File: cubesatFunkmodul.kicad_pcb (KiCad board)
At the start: 4 copper layers, 85 x 85 mm, 207 parts, among them CON11 DISCO-CON1, CON21 DISCO-CON2, Q1 SSM3J334RLFTR-ND, Q10 AO3414, Q11 MMBT5551-TP, Q12 MMBT5551-TP, Q13 MMBT5551-TP, Q14 MMBT5551-TP, Q15 MMBT5551-TP, Q16 MMBT5551-TP, Q17 AO3414, Q18 AO3414, Q2 AO3414, Q3 MMBT5551-TP, Q4 MMBT5551-TP, Q5 MMBT5551-TP, Q6 MMBT5551-TP, Q7 MMBT5551-TP, Q8 MMBT5551-TP, Q9 SSM3J334RLFTR-ND, U1 MC74HC4538A, U10 RFM23BP, U2 MAX892, U3 ATMEGA128-16AU, U4 LTC3113, U5 RFM23BP, U6 MC74HC4538A, U7 MAX892, U8 ATMEGA128-16AU, U9 LTC3113, Y1 Crystal_GND24, Y2 Crystal_GND24

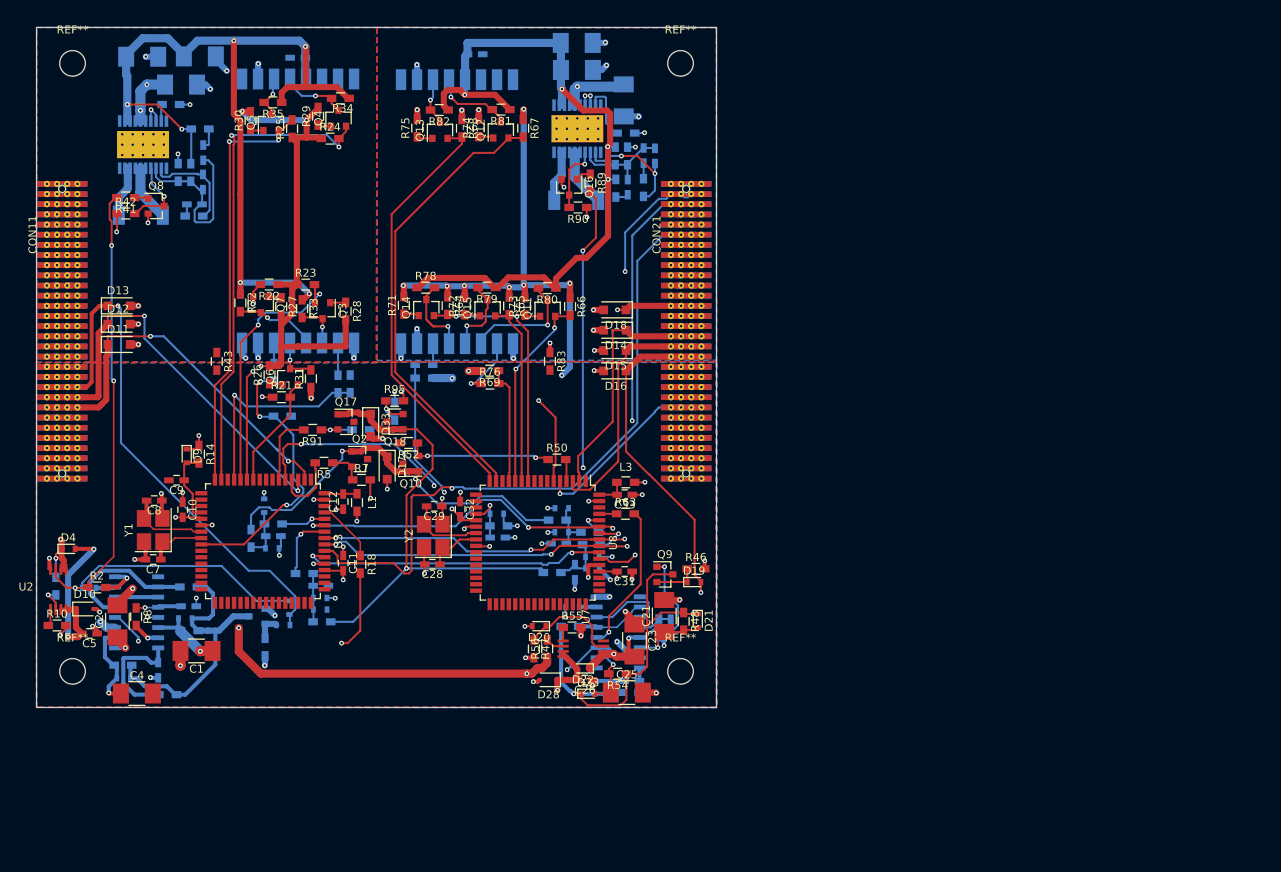
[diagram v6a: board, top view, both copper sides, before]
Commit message: Adds SMA and Burnwire connectors
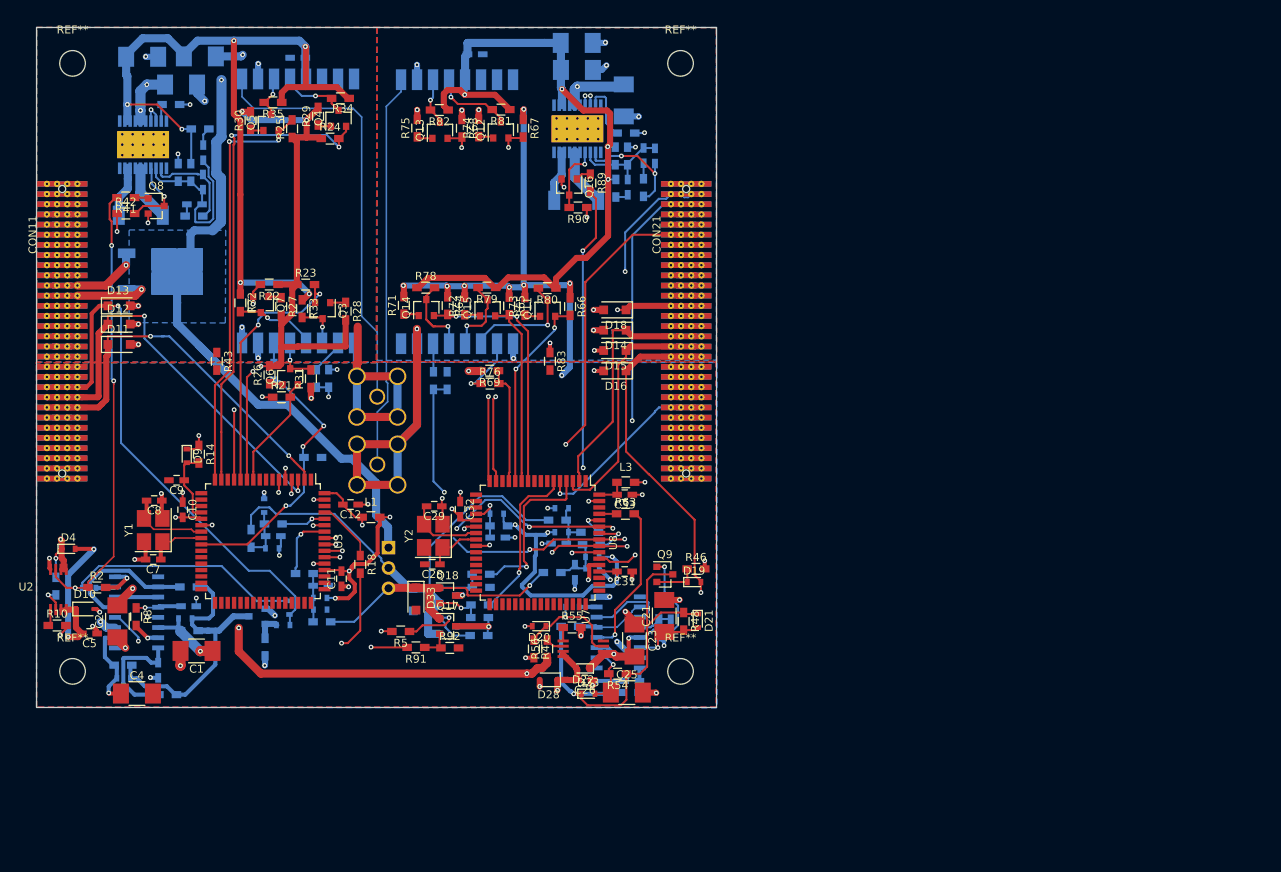
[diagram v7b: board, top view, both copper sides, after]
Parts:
- added AE1: Antenna, Connectors:SMA_THT_Jack_Straight, B.Cu at (93.6, 80.1)
- added AE2: Antenna, Connectors:SMA_THT_Jack_Straight, B.Cu at (93.6, 88.6)
- added D34: STPS640CBY-TR, TO_SOT_Packages_SMD:TO-252-2, B.Cu at (66.5, 64.5)
- added J1: Conn_01x03, Pin_Headers:Pin_Header_Straight_1x03_Pitch2.54mm, B.Cu at (95.0, 99.0)
- D17, Q10, Q2, R50, R52, R7, R95: moved to B.Cu
- R92: moved to F.Cu
- moved R91 30.1 mm to (98.4, 111.5)
- moved R92 29.4 mm to (102.7, 111.6)
- moved Q17 28.5 mm to (102.4, 108.8)
- moved R96 27.9 mm to (106.4, 107.8), turned to 0 degrees
- moved R95 27.6 mm to (106.4, 106.2)
- moved R7 24.4 mm to (106.3, 110.0)
- moved Q2 23.6 mm to (102.4, 108.9)
- moved R5 23.2 mm to (96.5, 109.5)
- moved Q18 22.7 mm to (102.4, 105.0), turned to 0 degrees
- moved D33 22.4 mm to (98.4, 105.4)
- moved R52 20.2 mm to (106.6, 104.0), turned to 0 degrees
- moved R50 17.2 mm to (106.5, 102.3)
- moved Q10 17.1 mm to (102.4, 105.0), turned to 0 degrees
- moved D17 16.8 mm to (98.1, 105.5)
- moved R44 6.41 mm to (85.5, 87.7)
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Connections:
- net Net-(CON21-Pad12) renamed /Connector/3V3_Reset
- CON11 pad 11: Net-(CON11-Pad11) -> /Connector/BAT1
- CON11 pad 12: Net-(CON11-Pad12) -> /Connector/BAT2
- U1 pad 9: (no net) -> Net-(U1-Pad9)
- U10 pad 14: (no net) -> Net-(U10-Pad14)
- U10 pad 15: (no net) -> Net-(U10-Pad15)
- U10 pad 16: (no net) -> Net-(U10-Pad16)
- U10 pad 9: (no net) -> Net-(AE2-Pad1)
- U3 pad 1: (no net) -> Net-(U3-Pad1)
- U3 pad 14: (no net) -> Net-(U3-Pad14)
- U3 pad 17: (no net) -> Net-(U3-Pad17)
- U3 pad 18: (no net) -> Net-(U3-Pad18)
- U3 pad 19: (no net) -> Net-(U3-Pad19)
- U3 pad 26: (no net) -> Net-(U3-Pad26)
- U3 pad 27: (no net) -> Net-(U3-Pad27)
- U3 pad 28: (no net) -> Net-(U3-Pad28)
- U3 pad 29: (no net) -> Net-(U3-Pad29)
- U3 pad 30: (no net) -> Net-(U3-Pad30)
- U3 pad 31: (no net) -> Net-(U3-Pad31)
- U3 pad 32: (no net) -> Net-(U3-Pad32)
- U3 pad 33: (no net) -> Net-(U3-Pad33)
- U3 pad 34: (no net) -> Net-(U3-Pad34)
- U3 pad 35: (no net) -> Net-(U3-Pad35)
- U3 pad 36: (no net) -> Net-(U3-Pad36)
- U3 pad 37: (no net) -> Net-(U3-Pad37)
- U3 pad 38: (no net) -> Net-(U3-Pad38)
- U3 pad 39: (no net) -> Net-(U3-Pad39)
- U3 pad 40: (no net) -> Net-(U3-Pad40)
- U3 pad 41: (no net) -> Net-(U3-Pad41)
- U3 pad 42: (no net) -> Net-(U3-Pad42)
- U3 pad 43: (no net) -> Net-(U3-Pad43)
- U3 pad 44: (no net) -> Net-(U3-Pad44)
- U3 pad 45: (no net) -> Net-(U3-Pad45)
- U3 pad 46: (no net) -> Net-(U3-Pad46)
- U3 pad 47: (no net) -> Net-(U3-Pad47)
- U3 pad 48: (no net) -> Net-(U3-Pad48)
- U3 pad 49: (no net) -> Net-(U3-Pad49)
- U3 pad 50: (no net) -> Net-(U3-Pad50)
- U3 pad 51: (no net) -> Net-(U3-Pad51)
- U3 pad 62: (no net) -> Net-(U3-Pad62)
- U3 pad 7: (no net) -> Net-(U3-Pad7)
- U3 pad 8: (no net) -> Net-(U3-Pad8)
- U3 pad 9: (no net) -> Net-(U3-Pad9)
- U5 pad 14: (no net) -> Net-(U5-Pad14)
- U5 pad 15: (no net) -> Net-(U5-Pad15)
- U5 pad 16: (no net) -> Net-(U5-Pad16)
- U5 pad 9: (no net) -> Net-(AE1-Pad1)
- U6 pad 9: (no net) -> Net-(U6-Pad9)
- U8 pad 1: (no net) -> Net-(U8-Pad1)
- U8 pad 14: (no net) -> Net-(U8-Pad14)
- U8 pad 17: (no net) -> Net-(U8-Pad17)
- U8 pad 18: (no net) -> Net-(U8-Pad18)
- U8 pad 19: (no net) -> Net-(U8-Pad19)
- U8 pad 26: (no net) -> Net-(U8-Pad26)
- U8 pad 27: (no net) -> Net-(U8-Pad27)
- U8 pad 28: (no net) -> Net-(U8-Pad28)
- U8 pad 29: (no net) -> Net-(U8-Pad29)
- U8 pad 30: (no net) -> Net-(U8-Pad30)
- U8 pad 31: (no net) -> Net-(U8-Pad31)
- U8 pad 32: (no net) -> Net-(U8-Pad32)
- U8 pad 33: (no net) -> Net-(U8-Pad33)
- U8 pad 34: (no net) -> Net-(U8-Pad34)
- U8 pad 35: (no net) -> Net-(U8-Pad35)
- U8 pad 36: (no net) -> Net-(U8-Pad36)
- U8 pad 37: (no net) -> Net-(U8-Pad37)
- U8 pad 38: (no net) -> Net-(U8-Pad38)
- U8 pad 39: (no net) -> Net-(U8-Pad39)
- U8 pad 40: (no net) -> Net-(U8-Pad40)
- U8 pad 41: (no net) -> Net-(U8-Pad41)
- U8 pad 42: (no net) -> Net-(U8-Pad42)
- U8 pad 43: (no net) -> Net-(U8-Pad43)
- U8 pad 44: (no net) -> Net-(U8-Pad44)
- U8 pad 45: (no net) -> Net-(U8-Pad45)
- U8 pad 46: (no net) -> Net-(U8-Pad46)
- U8 pad 47: (no net) -> Net-(U8-Pad47)
- U8 pad 48: (no net) -> Net-(U8-Pad48)
- U8 pad 49: (no net) -> Net-(U8-Pad49)
- U8 pad 50: (no net) -> Net-(U8-Pad50)
- U8 pad 51: (no net) -> Net-(U8-Pad51)
- U8 pad 62: (no net) -> Net-(U8-Pad62)
- U8 pad 7: (no net) -> Net-(U8-Pad7)
- U8 pad 8: (no net) -> Net-(U8-Pad8)
- U8 pad 9: (no net) -> Net-(U8-Pad9)
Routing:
- net VBAT: track 114.1 -> 194.4 mm, vias 5 -> 6
- net Net-(AE1-Pad1): track 0.00 -> 54.0 mm
- net Net-(AE2-Pad1): track 0.00 -> 49.5 mm
- net /Funkmodul2/Funkeinheit2/PGND: track 14.0 -> 61.5 mm, vias 8 -> 7
- net /Funkmodul1/Funkeinheit/PGND: track 13.6 -> 44.5 mm, vias 7 -> 6
- net /Funkmodul2/VCC: track 104.1 -> 132.3 mm
- net WIRE_CONN2: track 60.3 -> 34.7 mm
- net /Funkmodul1/BURNWIRE2: track 8.79 -> 30.5 mm, vias 0 -> 2
- net /Funkmodul2/BURNWIRE: track 2.73 -> 20.7 mm, vias 0 -> 1
- net /Funkmodul1/BURNWIRE: track 8.31 -> 25.0 mm, vias 0 -> 2
- net /Funkmodul1/VCC: track 100.6 -> 115.3 mm
- net /Connector/BAT2: track 0.00 -> 12.7 mm, vias 0 -> 1
- net Net-(Q10-Pad2): track 18.1 -> 5.74 mm, vias 2 -> 0
- net WIRE_CONN: track 49.7 -> 61.6 mm, vias 2 -> 0
- net /Funkmodul2/Funkeinheit2/RXON: track 57.4 -> 45.8 mm, vias 0 -> 2
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- added copper zone on In2.Cu, net /Funkmodul1/Funkeinheit/PGND
- added copper zone on In2.Cu, net /Funkmodul2/Funkeinheit2/PGND
- added copper zone on B.Cu, net VBAT

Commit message: Adds stiching vias
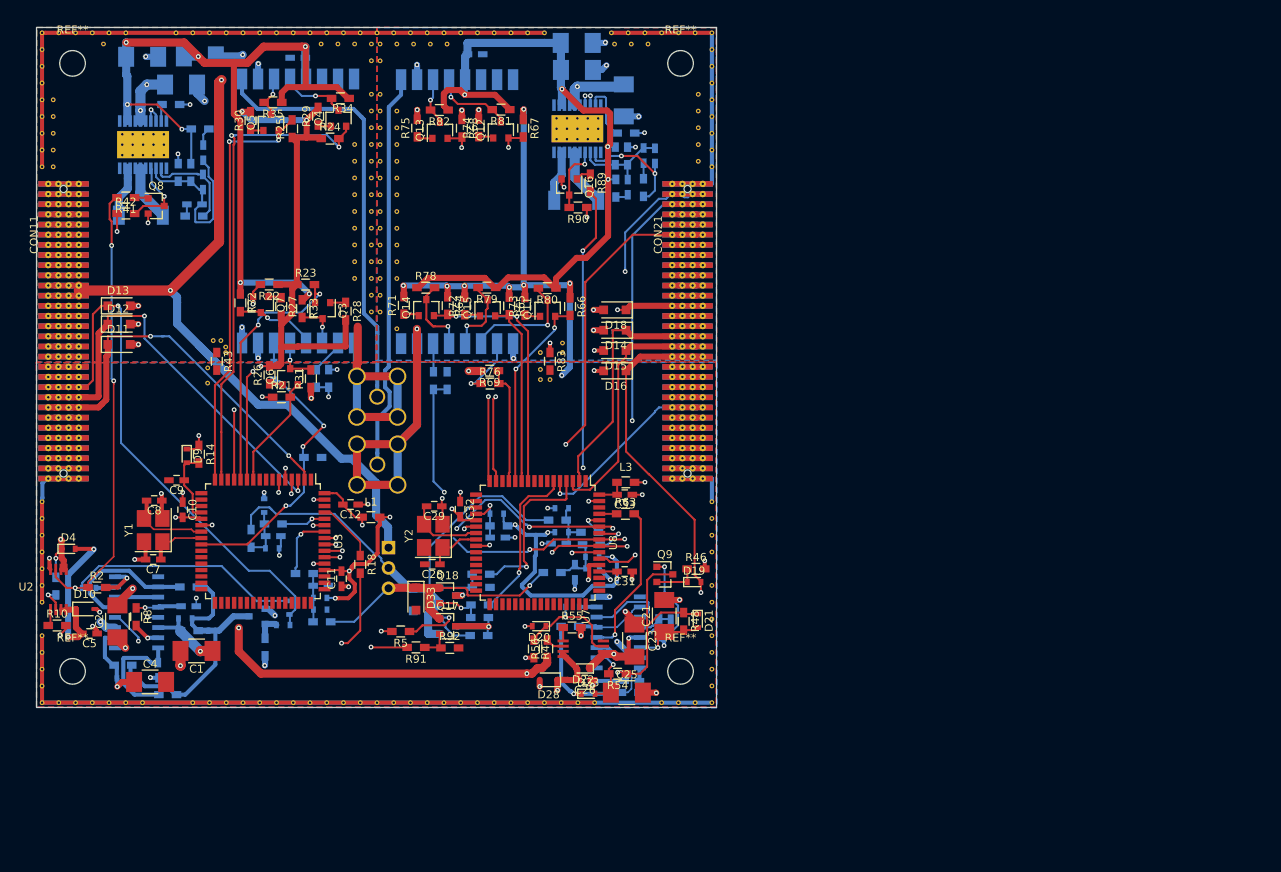
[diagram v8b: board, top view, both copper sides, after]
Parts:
- removed D34: STPS640CBY-TR, TO_SOT_Packages_SMD:TO-252-2
- added REF**: VIA-0.6, connect-sm:VIA-0.6, F.Cu at (115.2, 78.0)
- added REF**: VIA-0.6, connect-sm:VIA-0.6, F.Cu at (74.6, 74.6)
- added REF**: VIA-0.6, connect-sm:VIA-0.6, F.Cu at (51.7, 110.0)
- added REF**: VIA-0.6, connect-sm:VIA-0.6, F.Cu at (51.7, 112.1)
- added REF**: VIA-0.6, connect-sm:VIA-0.6, F.Cu at (51.7, 114.2)
- added REF**: VIA-0.6, connect-sm:VIA-0.6, F.Cu at (51.7, 116.3)
- added REF**: VIA-0.6, connect-sm:VIA-0.6, F.Cu at (51.7, 118.4)
- added REF**: VIA-0.6, connect-sm:VIA-0.6, F.Cu at (53.8, 118.4)
- added REF**: VIA-0.6, connect-sm:VIA-0.6, F.Cu at (55.9, 118.4)
- added REF**: VIA-0.6, connect-sm:VIA-0.6, F.Cu at (58.0, 118.4)
- added REF**: VIA-0.6, connect-sm:VIA-0.6, F.Cu at (60.1, 118.4)
- added REF**: VIA-0.6, connect-sm:VIA-0.6, F.Cu at (62.2, 118.4)
- added REF**: VIA-0.6, connect-sm:VIA-0.6, F.Cu at (74.0, 73.1)
- added REF**: VIA-0.6, connect-sm:VIA-0.6, F.Cu at (64.2, 118.4)
- added REF**: VIA-0.6, connect-sm:VIA-0.6, F.Cu at (70.5, 118.4)
- added REF**: VIA-0.6, connect-sm:VIA-0.6, F.Cu at (72.6, 118.4)
- added REF**: VIA-0.6, connect-sm:VIA-0.6, F.Cu at (74.7, 118.4)
- added REF**: VIA-0.6, connect-sm:VIA-0.6, F.Cu at (76.8, 118.4)
- added REF**: VIA-0.6, connect-sm:VIA-0.6, F.Cu at (78.9, 118.4)
- added REF**: VIA-0.6, connect-sm:VIA-0.6, F.Cu at (81.0, 118.4)
- added REF**: VIA-0.6, connect-sm:VIA-0.6, F.Cu at (83.1, 118.4)
- added REF**: VIA-0.6, connect-sm:VIA-0.6, F.Cu at (85.2, 118.4)
- added REF**: VIA-0.6, connect-sm:VIA-0.6, F.Cu at (87.3, 118.4)
- added REF**: VIA-0.6, connect-sm:VIA-0.6, F.Cu at (133.7, 50.7)
- added REF**: VIA-0.6, connect-sm:VIA-0.6, F.Cu at (89.4, 118.4)
- added REF**: VIA-0.6, connect-sm:VIA-0.6, F.Cu at (91.5, 118.4)
- added REF**: VIA-0.6, connect-sm:VIA-0.6, F.Cu at (93.6, 118.4)
- added REF**: VIA-0.6, connect-sm:VIA-0.6, F.Cu at (95.6, 118.4)
- added REF**: VIA-0.6, connect-sm:VIA-0.6, F.Cu at (97.7, 118.4)
- added REF**: VIA-0.6, connect-sm:VIA-0.6, F.Cu at (99.8, 118.4)
- added REF**: VIA-0.6, connect-sm:VIA-0.6, F.Cu at (101.9, 118.4)
- added REF**: VIA-0.6, connect-sm:VIA-0.6, F.Cu at (104.0, 118.4)
- added REF**: VIA-0.6, connect-sm:VIA-0.6, F.Cu at (106.1, 118.4)
- added REF**: VIA-0.6, connect-sm:VIA-0.6, F.Cu at (108.2, 118.4)
- added REF**: VIA-0.6, connect-sm:VIA-0.6, F.Cu at (133.7, 48.6)
- added REF**: VIA-0.6, connect-sm:VIA-0.6, F.Cu at (110.3, 118.4)
- added REF**: VIA-0.6, connect-sm:VIA-0.6, F.Cu at (112.4, 118.4)
- added REF**: VIA-0.6, connect-sm:VIA-0.6, F.Cu at (114.5, 118.4)
- added REF**: VIA-0.6, connect-sm:VIA-0.6, F.Cu at (116.6, 118.4)
- added REF**: VIA-0.6, connect-sm:VIA-0.6, F.Cu at (118.7, 118.4)
- added REF**: VIA-0.6, connect-sm:VIA-0.6, F.Cu at (120.8, 118.4)
- added REF**: VIA-0.6, connect-sm:VIA-0.6, F.Cu at (129.1, 118.4)
- added REF**: VIA-0.6, connect-sm:VIA-0.6, F.Cu at (131.2, 118.4)
- added REF**: VIA-0.6, connect-sm:VIA-0.6, F.Cu at (133.3, 118.4)
- added REF**: VIA-0.6, connect-sm:VIA-0.6, F.Cu at (135.4, 118.4)
- added REF**: VIA-0.6, connect-sm:VIA-0.6, F.Cu at (133.7, 46.5)
- added REF**: VIA-0.6, connect-sm:VIA-0.6, F.Cu at (135.4, 116.3)
- added REF**: VIA-0.6, connect-sm:VIA-0.6, F.Cu at (135.4, 114.2)
- added REF**: VIA-0.6, connect-sm:VIA-0.6, F.Cu at (135.4, 112.1)
- added REF**: VIA-0.6, connect-sm:VIA-0.6, F.Cu at (135.4, 110.0)
- added REF**: VIA-0.6, connect-sm:VIA-0.6, F.Cu at (135.4, 107.9)
- added REF**: VIA-0.6, connect-sm:VIA-0.6, F.Cu at (135.4, 105.8)
- added REF**: VIA-0.6, connect-sm:VIA-0.6, F.Cu at (135.4, 103.7)
- added REF**: VIA-0.6, connect-sm:VIA-0.6, F.Cu at (135.4, 99.6)
- added REF**: VIA-0.6, connect-sm:VIA-0.6, F.Cu at (135.4, 97.5)
- added REF**: VIA-0.6, connect-sm:VIA-0.6, F.Cu at (135.4, 95.4)
- added REF**: VIA-0.6, connect-sm:VIA-0.6, F.Cu at (133.7, 44.4)
- added REF**: VIA-0.6, connect-sm:VIA-0.6, F.Cu at (135.4, 93.3)
- added REF**: VIA-0.6, connect-sm:VIA-0.6, F.Cu at (135.4, 51.4)
- added REF**: VIA-0.6, connect-sm:VIA-0.6, F.Cu at (135.4, 49.3)
- added REF**: VIA-0.6, connect-sm:VIA-0.6, F.Cu at (135.4, 47.2)
- added REF**: VIA-0.6, connect-sm:VIA-0.6, F.Cu at (135.4, 45.1)
- added REF**: VIA-0.6, connect-sm:VIA-0.6, F.Cu at (135.4, 43.0)
- added REF**: VIA-0.6, connect-sm:VIA-0.6, F.Cu at (135.4, 41.0)
- added REF**: VIA-0.6, connect-sm:VIA-0.6, F.Cu at (135.4, 38.9)
- added REF**: VIA-0.6, connect-sm:VIA-0.6, F.Cu at (135.4, 36.8)
- added REF**: VIA-0.6, connect-sm:VIA-0.6, F.Cu at (135.4, 34.7)
- added REF**: VIA-0.6, connect-sm:VIA-0.6, F.Cu at (133.7, 42.4)
- added REF**: VIA-0.6, connect-sm:VIA-0.6, F.Cu at (133.3, 34.7)
- added REF**: VIA-0.6, connect-sm:VIA-0.6, F.Cu at (131.2, 34.7)
- added REF**: VIA-0.6, connect-sm:VIA-0.6, F.Cu at (129.1, 34.7)
- added REF**: VIA-0.6, connect-sm:VIA-0.6, F.Cu at (127.0, 34.7)
- added REF**: VIA-0.6, connect-sm:VIA-0.6, F.Cu at (125.0, 34.7)
- added REF**: VIA-0.6, connect-sm:VIA-0.6, F.Cu at (122.9, 34.7)
- added REF**: VIA-0.6, connect-sm:VIA-0.6, F.Cu at (114.5, 34.7)
- added REF**: VIA-0.6, connect-sm:VIA-0.6, F.Cu at (112.4, 34.7)
- added REF**: VIA-0.6, connect-sm:VIA-0.6, F.Cu at (110.3, 34.7)
- added REF**: VIA-0.6, connect-sm:VIA-0.6, F.Cu at (108.2, 34.7)
- added REF**: VIA-0.6, connect-sm:VIA-0.6, F.Cu at (127.4, 36.1)
- added REF**: VIA-0.6, connect-sm:VIA-0.6, F.Cu at (106.1, 34.7)
- added REF**: VIA-0.6, connect-sm:VIA-0.6, F.Cu at (104.0, 34.7)
- added REF**: VIA-0.6, connect-sm:VIA-0.6, F.Cu at (101.9, 34.7)
- added REF**: VIA-0.6, connect-sm:VIA-0.6, F.Cu at (99.8, 34.7)
- added REF**: VIA-0.6, connect-sm:VIA-0.6, F.Cu at (97.7, 34.7)
- added REF**: VIA-0.6, connect-sm:VIA-0.6, F.Cu at (95.6, 34.7)
- added REF**: VIA-0.6, connect-sm:VIA-0.6, F.Cu at (93.6, 34.7)
- added REF**: VIA-0.6, connect-sm:VIA-0.6, F.Cu at (91.5, 34.7)
- added REF**: VIA-0.6, connect-sm:VIA-0.6, F.Cu at (89.4, 34.7)
- added REF**: VIA-0.6, connect-sm:VIA-0.6, F.Cu at (87.3, 34.7)
- added REF**: VIA-0.6, connect-sm:VIA-0.6, F.Cu at (125.3, 36.1)
- added REF**: VIA-0.6, connect-sm:VIA-0.6, F.Cu at (85.2, 34.7)
- added REF**: VIA-0.6, connect-sm:VIA-0.6, F.Cu at (83.1, 34.7)
- added REF**: VIA-0.6, connect-sm:VIA-0.6, F.Cu at (81.0, 34.7)
- added REF**: VIA-0.6, connect-sm:VIA-0.6, F.Cu at (78.9, 34.7)
- added REF**: VIA-0.6, connect-sm:VIA-0.6, F.Cu at (76.8, 34.7)
- added REF**: VIA-0.6, connect-sm:VIA-0.6, F.Cu at (74.7, 34.7)
- added REF**: VIA-0.6, connect-sm:VIA-0.6, F.Cu at (72.6, 34.7)
- added REF**: VIA-0.6, connect-sm:VIA-0.6, F.Cu at (70.5, 34.7)
- added REF**: VIA-0.6, connect-sm:VIA-0.6, F.Cu at (68.4, 34.7)
- added REF**: VIA-0.6, connect-sm:VIA-0.6, F.Cu at (62.2, 34.7)
- added REF**: VIA-0.6, connect-sm:VIA-0.6, F.Cu at (123.2, 36.1)
- added REF**: VIA-0.6, connect-sm:VIA-0.6, F.Cu at (60.1, 34.7)
- added REF**: VIA-0.6, connect-sm:VIA-0.6, F.Cu at (58.0, 34.7)
- added REF**: VIA-0.6, connect-sm:VIA-0.6, F.Cu at (55.9, 34.7)
- added REF**: VIA-0.6, connect-sm:VIA-0.6, F.Cu at (53.8, 34.7)
- added REF**: VIA-0.6, connect-sm:VIA-0.6, F.Cu at (51.7, 34.7)
- added REF**: VIA-0.6, connect-sm:VIA-0.6, F.Cu at (53.1, 51.4)
- added REF**: VIA-0.6, connect-sm:VIA-0.6, F.Cu at (114.0, 78.0)
- added REF**: VIA-0.6, connect-sm:VIA-0.6, F.Cu at (102.3, 36.1)
- added REF**: VIA-0.6, connect-sm:VIA-0.6, F.Cu at (73.1, 73.1)
- added REF**: VIA-0.6, connect-sm:VIA-0.6, F.Cu at (100.2, 36.1)
- added REF**: VIA-0.6, connect-sm:VIA-0.6, F.Cu at (98.1, 36.1)
- added REF**: VIA-0.6, connect-sm:VIA-0.6, F.Cu at (96.0, 36.1)
- added REF**: VIA-0.6, connect-sm:VIA-0.6, F.Cu at (96.0, 71.7)
- added REF**: VIA-0.6, connect-sm:VIA-0.6, F.Cu at (96.0, 65.4)
- added REF**: VIA-0.6, connect-sm:VIA-0.6, F.Cu at (96.0, 63.3)
- added REF**: VIA-0.6, connect-sm:VIA-0.6, F.Cu at (96.0, 61.2)
- added REF**: VIA-0.6, connect-sm:VIA-0.6, F.Cu at (96.0, 59.1)
- added REF**: VIA-0.6, connect-sm:VIA-0.6, F.Cu at (96.0, 57.0)
- added REF**: VIA-0.6, connect-sm:VIA-0.6, F.Cu at (114.0, 76.7)
- added REF**: VIA-0.6, connect-sm:VIA-0.6, F.Cu at (96.0, 54.9)
- added REF**: VIA-0.6, connect-sm:VIA-0.6, F.Cu at (96.0, 52.8)
- added REF**: VIA-0.6, connect-sm:VIA-0.6, F.Cu at (96.0, 50.7)
- added REF**: VIA-0.6, connect-sm:VIA-0.6, F.Cu at (96.0, 48.6)
- added REF**: VIA-0.6, connect-sm:VIA-0.6, F.Cu at (96.0, 46.5)
- added REF**: VIA-0.6, connect-sm:VIA-0.6, F.Cu at (96.0, 44.4)
- added REF**: VIA-0.6, connect-sm:VIA-0.6, F.Cu at (93.9, 69.6)
- added REF**: VIA-0.6, connect-sm:VIA-0.6, F.Cu at (93.9, 67.5)
- added REF**: VIA-0.6, connect-sm:VIA-0.6, F.Cu at (93.9, 65.4)
- added REF**: VIA-0.6, connect-sm:VIA-0.6, F.Cu at (93.9, 63.3)
- added REF**: VIA-0.6, connect-sm:VIA-0.6, F.Cu at (116.7, 73.4)
- added REF**: VIA-0.6, connect-sm:VIA-0.6, F.Cu at (93.9, 61.2)
- added REF**: VIA-0.6, connect-sm:VIA-0.6, F.Cu at (93.9, 59.1)
- added REF**: VIA-0.6, connect-sm:VIA-0.6, F.Cu at (93.9, 57.0)
- added REF**: VIA-0.6, connect-sm:VIA-0.6, F.Cu at (93.9, 54.9)
- added REF**: VIA-0.6, connect-sm:VIA-0.6, F.Cu at (93.9, 52.8)
- added REF**: VIA-0.6, connect-sm:VIA-0.6, F.Cu at (93.9, 50.7)
- added REF**: VIA-0.6, connect-sm:VIA-0.6, F.Cu at (93.9, 48.6)
- added REF**: VIA-0.6, connect-sm:VIA-0.6, F.Cu at (93.9, 46.5)
- added REF**: VIA-0.6, connect-sm:VIA-0.6, F.Cu at (93.9, 44.4)
- added REF**: VIA-0.6, connect-sm:VIA-0.6, F.Cu at (93.9, 42.4)
- added REF**: VIA-0.6, connect-sm:VIA-0.6, F.Cu at (116.7, 74.6)
- added REF**: VIA-0.6, connect-sm:VIA-0.6, F.Cu at (93.9, 38.2)
- added REF**: VIA-0.6, connect-sm:VIA-0.6, F.Cu at (93.9, 36.1)
- added REF**: VIA-0.6, connect-sm:VIA-0.6, F.Cu at (90.8, 48.6)
- added REF**: VIA-0.6, connect-sm:VIA-0.6, F.Cu at (90.8, 50.7)
- added REF**: VIA-0.6, connect-sm:VIA-0.6, F.Cu at (90.8, 52.8)
- added REF**: VIA-0.6, connect-sm:VIA-0.6, F.Cu at (90.8, 54.9)
- added REF**: VIA-0.6, connect-sm:VIA-0.6, F.Cu at (90.8, 57.0)
- added REF**: VIA-0.6, connect-sm:VIA-0.6, F.Cu at (90.8, 59.1)
- added REF**: VIA-0.6, connect-sm:VIA-0.6, F.Cu at (90.8, 61.2)
- added REF**: VIA-0.6, connect-sm:VIA-0.6, F.Cu at (90.8, 63.3)
- added REF**: VIA-0.6, connect-sm:VIA-0.6, F.Cu at (114.0, 74.6)
- added REF**: VIA-0.6, connect-sm:VIA-0.6, F.Cu at (90.8, 65.4)
- added REF**: VIA-0.6, connect-sm:VIA-0.6, F.Cu at (92.9, 69.6)
- added REF**: VIA-0.6, connect-sm:VIA-0.6, F.Cu at (92.9, 67.5)
- added REF**: VIA-0.6, connect-sm:VIA-0.6, F.Cu at (92.9, 65.4)
- added REF**: VIA-0.6, connect-sm:VIA-0.6, F.Cu at (92.9, 63.3)
- added REF**: VIA-0.6, connect-sm:VIA-0.6, F.Cu at (92.9, 61.2)
- added REF**: VIA-0.6, connect-sm:VIA-0.6, F.Cu at (92.9, 59.1)
- added REF**: VIA-0.6, connect-sm:VIA-0.6, F.Cu at (92.9, 57.0)
- added REF**: VIA-0.6, connect-sm:VIA-0.6, F.Cu at (92.9, 54.9)
- added REF**: VIA-0.6, connect-sm:VIA-0.6, F.Cu at (92.9, 52.8)
- added REF**: VIA-0.6, connect-sm:VIA-0.6, F.Cu at (72.4, 78.5)
- added REF**: VIA-0.6, connect-sm:VIA-0.6, F.Cu at (92.9, 50.7)
- added REF**: VIA-0.6, connect-sm:VIA-0.6, F.Cu at (92.9, 48.6)
- added REF**: VIA-0.6, connect-sm:VIA-0.6, F.Cu at (92.9, 46.5)
- added REF**: VIA-0.6, connect-sm:VIA-0.6, F.Cu at (92.9, 44.4)
- added REF**: VIA-0.6, connect-sm:VIA-0.6, F.Cu at (92.9, 42.3)
- added REF**: VIA-0.6, connect-sm:VIA-0.6, F.Cu at (92.9, 38.2)
- added REF**: VIA-0.6, connect-sm:VIA-0.6, F.Cu at (92.9, 36.1)
- added REF**: VIA-0.6, connect-sm:VIA-0.6, F.Cu at (90.8, 36.1)
- added REF**: VIA-0.6, connect-sm:VIA-0.6, F.Cu at (88.7, 36.1)
- added REF**: VIA-0.6, connect-sm:VIA-0.6, F.Cu at (86.6, 36.1)
- added REF**: VIA-0.6, connect-sm:VIA-0.6, F.Cu at (72.4, 76.6)
- added REF**: VIA-0.6, connect-sm:VIA-0.6, F.Cu at (59.4, 36.1)
- added REF**: VIA-0.6, connect-sm:VIA-0.6, F.Cu at (53.1, 43.0)
- added REF**: VIA-0.6, connect-sm:VIA-0.6, F.Cu at (53.1, 45.1)
- added REF**: VIA-0.6, connect-sm:VIA-0.6, F.Cu at (53.1, 47.2)
- added REF**: VIA-0.6, connect-sm:VIA-0.6, F.Cu at (53.1, 49.3)
- added REF**: VIA-0.6, connect-sm:VIA-0.6, F.Cu at (51.7, 36.8)
- added REF**: VIA-0.6, connect-sm:VIA-0.6, F.Cu at (51.7, 38.9)
- added REF**: VIA-0.6, connect-sm:VIA-0.6, F.Cu at (51.7, 41.0)
- added REF**: VIA-0.6, connect-sm:VIA-0.6, F.Cu at (51.7, 43.0)
- added REF**: VIA-0.6, connect-sm:VIA-0.6, F.Cu at (51.7, 45.1)
- added REF**: VIA-0.6, connect-sm:VIA-0.6, F.Cu at (74.6, 73.9)
- added REF**: VIA-0.6, connect-sm:VIA-0.6, F.Cu at (51.7, 47.2)
- added REF**: VIA-0.6, connect-sm:VIA-0.6, F.Cu at (51.7, 49.3)
- added REF**: VIA-0.6, connect-sm:VIA-0.6, F.Cu at (51.7, 51.4)
- added REF**: VIA-0.6, connect-sm:VIA-0.6, F.Cu at (51.7, 93.3)
- added REF**: VIA-0.6, connect-sm:VIA-0.6, F.Cu at (51.7, 95.4)
- added REF**: VIA-0.6, connect-sm:VIA-0.6, F.Cu at (51.7, 97.5)
- added REF**: VIA-0.6, connect-sm:VIA-0.6, F.Cu at (51.7, 99.6)
- added REF**: VIA-0.6, connect-sm:VIA-0.6, F.Cu at (51.7, 101.7)
- added REF**: VIA-0.6, connect-sm:VIA-0.6, F.Cu at (51.7, 103.7)
- added REF**: VIA-0.6, connect-sm:VIA-0.6, F.Cu at (51.7, 105.8)
- moved C4 2.19 mm to (65.2, 115.8)
- moved CON11 0.17 mm to (54.5, 72.0)
- moved CON21 0.17 mm to (132.5, 72.0)
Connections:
- CON11 pad 11: /Connector/BAT1 -> VBAT
- CON11 pad 12: /Connector/BAT2 -> VBAT
- U1 pad 9: Net-(U1-Pad9) -> (no net)
- U10 pad 14: Net-(U10-Pad14) -> (no net)
- U10 pad 15: Net-(U10-Pad15) -> (no net)
- U10 pad 16: Net-(U10-Pad16) -> (no net)
- U3 pad 1: Net-(U3-Pad1) -> (no net)
- U3 pad 14: Net-(U3-Pad14) -> (no net)
- U3 pad 17: Net-(U3-Pad17) -> (no net)
- U3 pad 18: Net-(U3-Pad18) -> (no net)
- U3 pad 19: Net-(U3-Pad19) -> (no net)
- U3 pad 26: Net-(U3-Pad26) -> (no net)
- U3 pad 27: Net-(U3-Pad27) -> (no net)
- U3 pad 28: Net-(U3-Pad28) -> (no net)
- U3 pad 29: Net-(U3-Pad29) -> (no net)
- U3 pad 30: Net-(U3-Pad30) -> (no net)
- U3 pad 31: Net-(U3-Pad31) -> (no net)
- U3 pad 32: Net-(U3-Pad32) -> (no net)
- U3 pad 33: Net-(U3-Pad33) -> (no net)
- U3 pad 34: Net-(U3-Pad34) -> (no net)
- U3 pad 35: Net-(U3-Pad35) -> (no net)
- U3 pad 36: Net-(U3-Pad36) -> (no net)
- U3 pad 37: Net-(U3-Pad37) -> (no net)
- U3 pad 38: Net-(U3-Pad38) -> (no net)
- U3 pad 39: Net-(U3-Pad39) -> (no net)
- U3 pad 40: Net-(U3-Pad40) -> (no net)
- U3 pad 41: Net-(U3-Pad41) -> (no net)
- U3 pad 42: Net-(U3-Pad42) -> (no net)
- U3 pad 43: Net-(U3-Pad43) -> (no net)
- U3 pad 44: Net-(U3-Pad44) -> (no net)
- U3 pad 45: Net-(U3-Pad45) -> (no net)
- U3 pad 46: Net-(U3-Pad46) -> (no net)
- U3 pad 47: Net-(U3-Pad47) -> (no net)
- U3 pad 48: Net-(U3-Pad48) -> (no net)
- U3 pad 49: Net-(U3-Pad49) -> (no net)
- U3 pad 50: Net-(U3-Pad50) -> (no net)
- U3 pad 51: Net-(U3-Pad51) -> (no net)
- U3 pad 62: Net-(U3-Pad62) -> (no net)
- U3 pad 7: Net-(U3-Pad7) -> (no net)
- U3 pad 8: Net-(U3-Pad8) -> (no net)
- U3 pad 9: Net-(U3-Pad9) -> (no net)
- U5 pad 14: Net-(U5-Pad14) -> (no net)
- U5 pad 15: Net-(U5-Pad15) -> (no net)
- U5 pad 16: Net-(U5-Pad16) -> (no net)
- U6 pad 9: Net-(U6-Pad9) -> (no net)
- U8 pad 1: Net-(U8-Pad1) -> (no net)
- U8 pad 14: Net-(U8-Pad14) -> (no net)
- U8 pad 17: Net-(U8-Pad17) -> (no net)
- U8 pad 18: Net-(U8-Pad18) -> (no net)
- U8 pad 19: Net-(U8-Pad19) -> (no net)
- U8 pad 26: Net-(U8-Pad26) -> (no net)
- U8 pad 27: Net-(U8-Pad27) -> (no net)
- U8 pad 28: Net-(U8-Pad28) -> (no net)
- U8 pad 29: Net-(U8-Pad29) -> (no net)
- U8 pad 30: Net-(U8-Pad30) -> (no net)
- U8 pad 31: Net-(U8-Pad31) -> (no net)
- U8 pad 32: Net-(U8-Pad32) -> (no net)
- U8 pad 33: Net-(U8-Pad33) -> (no net)
- U8 pad 34: Net-(U8-Pad34) -> (no net)
- U8 pad 35: Net-(U8-Pad35) -> (no net)
- U8 pad 36: Net-(U8-Pad36) -> (no net)
- U8 pad 37: Net-(U8-Pad37) -> (no net)
- U8 pad 38: Net-(U8-Pad38) -> (no net)
- U8 pad 39: Net-(U8-Pad39) -> (no net)
- U8 pad 40: Net-(U8-Pad40) -> (no net)
- U8 pad 41: Net-(U8-Pad41) -> (no net)
- U8 pad 42: Net-(U8-Pad42) -> (no net)
- U8 pad 43: Net-(U8-Pad43) -> (no net)
- U8 pad 44: Net-(U8-Pad44) -> (no net)
- U8 pad 45: Net-(U8-Pad45) -> (no net)
- U8 pad 46: Net-(U8-Pad46) -> (no net)
- U8 pad 47: Net-(U8-Pad47) -> (no net)
- U8 pad 48: Net-(U8-Pad48) -> (no net)
- U8 pad 49: Net-(U8-Pad49) -> (no net)
- U8 pad 50: Net-(U8-Pad50) -> (no net)
- U8 pad 51: Net-(U8-Pad51) -> (no net)
- U8 pad 62: Net-(U8-Pad62) -> (no net)
- U8 pad 7: Net-(U8-Pad7) -> (no net)
- U8 pad 8: Net-(U8-Pad8) -> (no net)
- U8 pad 9: Net-(U8-Pad9) -> (no net)
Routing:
- net GND: track 117.1 -> 716.0 mm
- net VBAT: track 194.4 -> 213.3 mm, vias 6 -> 7
- net /Connector/BAT2: track 12.7 -> 0.00 mm, vias 1 -> 0
- net /Connector/BAT1: track 11.2 -> 0.00 mm, vias 1 -> 0
- net Net-(D21-Pad1): track 50.7 -> 46.7 mm, vias 1 -> 2
- net Net-(C4-Pad1): track 11.4 -> 10.5 mm
- net /Connector/~ENABLE1~: track 69.1 -> 69.9 mm
- net /Funkmodul1/Funkeinheit/5V: vias 7 -> 8
- removed copper zone on B.Cu, net VBAT
